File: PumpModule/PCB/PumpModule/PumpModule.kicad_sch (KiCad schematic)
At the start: 8 parts, among them J5 Conn_01x04, J6 Conn_01x04, J7 Conn_01x03

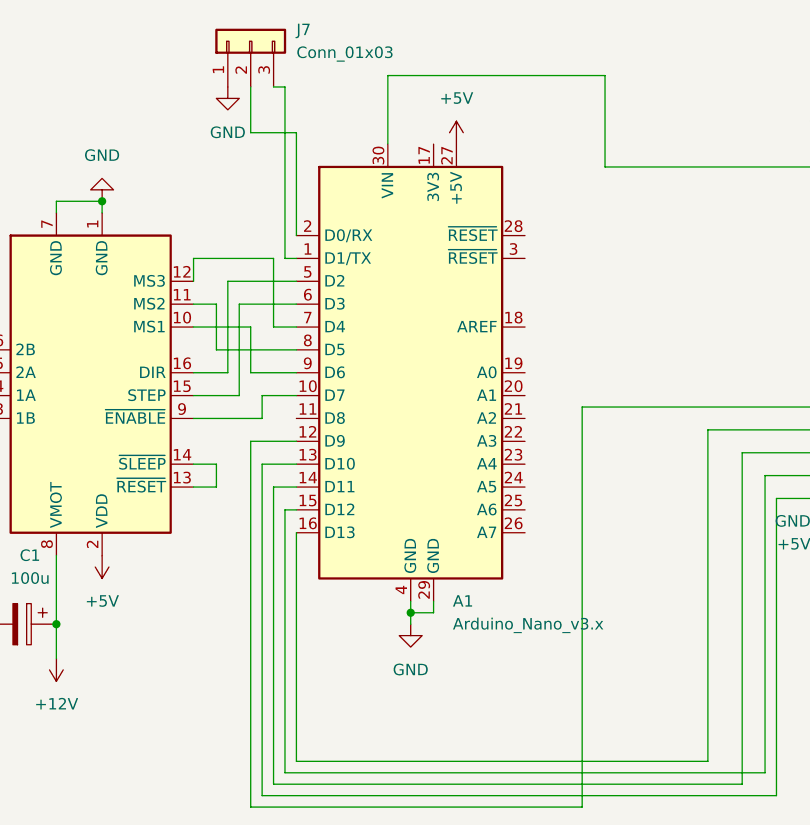
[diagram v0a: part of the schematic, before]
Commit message: [PCB][Pump Module] Fixed PCB pinout
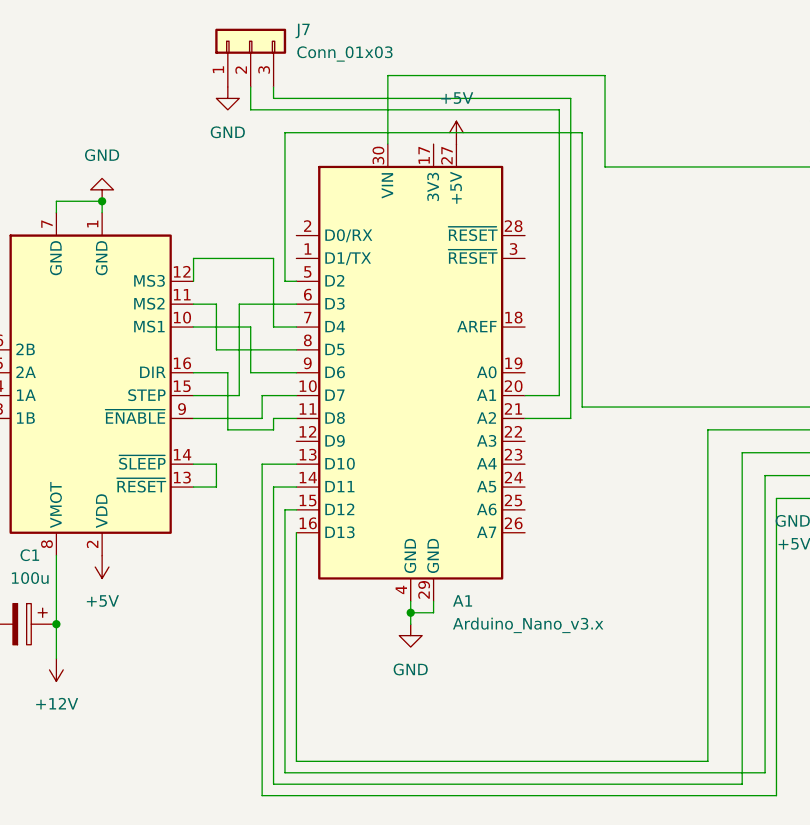
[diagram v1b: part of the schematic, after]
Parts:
- MCP2515Module1, U1: value ~ -> (none)
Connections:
- net at A2.16 (DIR): now also A1.11 (D8); no longer A1.5 (D2)
- net at A1.1 (D1/TX): no longer J7.3 (Pin_3)
- net at A1.12 (D9): no longer MCP2515Module1.7 (INT)
- net at A1.2 (D0/RX): no longer J7.2 (Pin_2)
- net at A1.20 (A1): now also J7.2 (Pin_2)
- net at A1.21 (A2): now also J7.3 (Pin_3)
- new net: A1.5 (D2), MCP2515Module1.7 (INT)

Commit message: [PCB] Made Pump v1.0 PCB
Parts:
- added D1: LED, LED_THT:LED_D2.0mm_W4.8mm_H2.5mm_FlatTop, symbol Device:LED
- added R1: R, Resistor_THT:R_Axial_DIN0204_L3.6mm_D1.6mm_P7.62mm_Horizontal, symbol Device:R
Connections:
- net GND: now also J7.3 (Pin_3), D1.1 (K); no longer J7.1 (Pin_1)
- net at A1.12 (D9): now also R1.1
- net at A1.21 (A2): now also J7.1 (Pin_1); no longer J7.3 (Pin_3)
- new net: D1.2 (A), R1.2

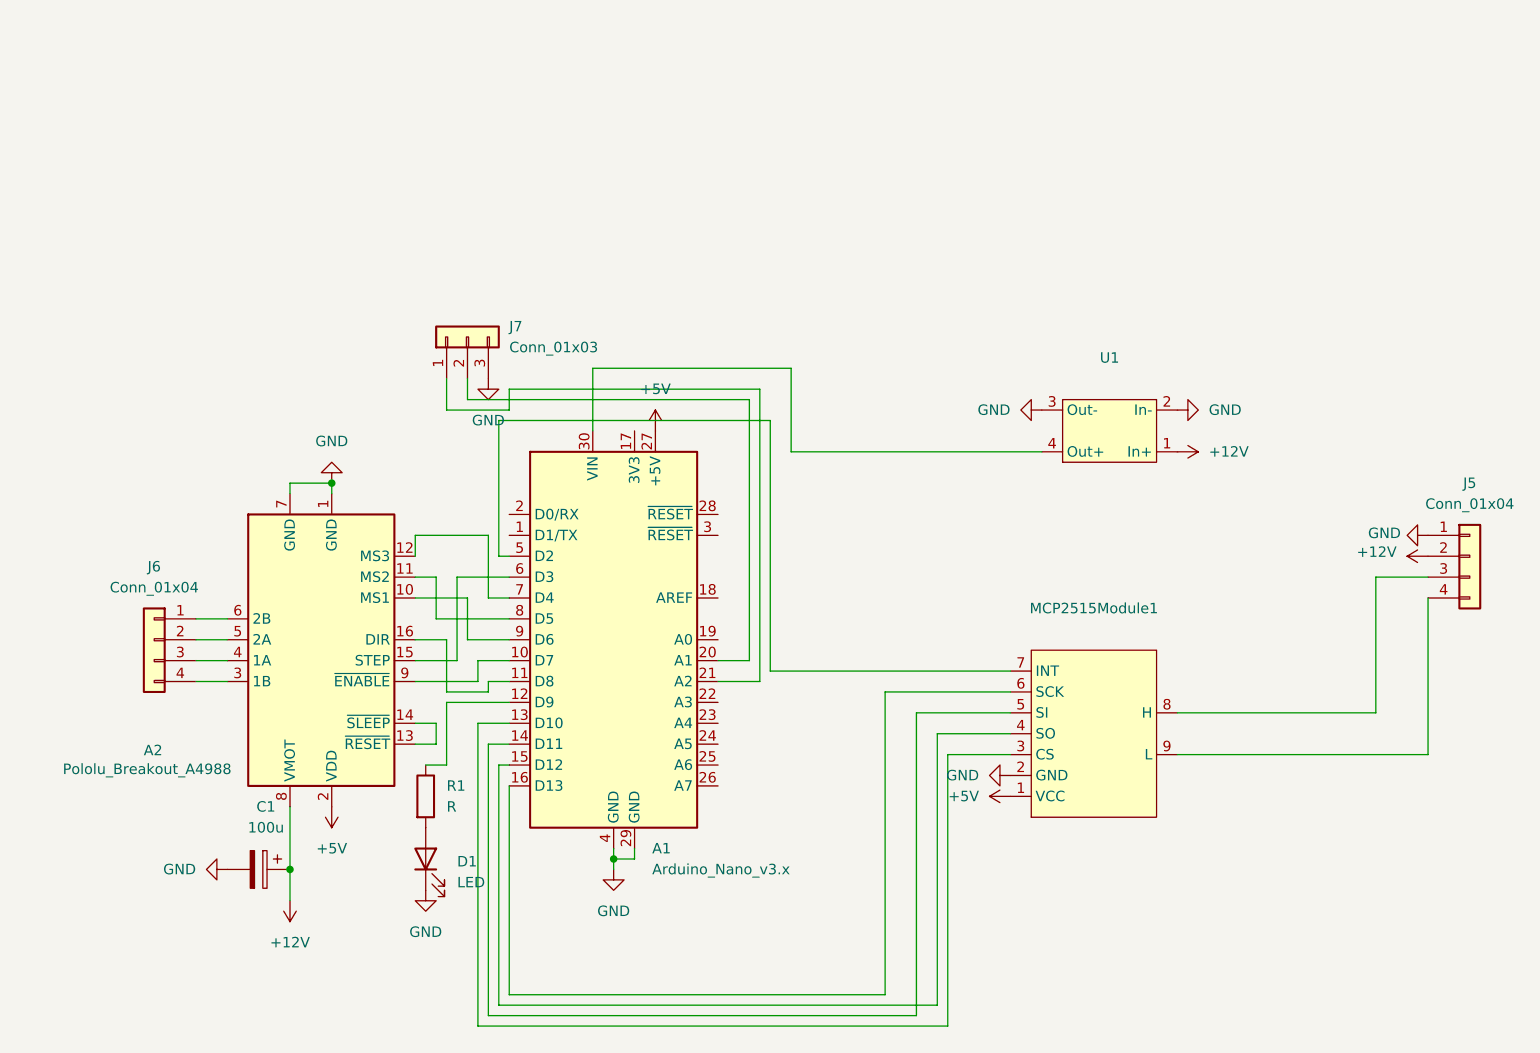
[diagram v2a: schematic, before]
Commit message: [PCB][PumpModule] Fixed input power pinout. Changed indication pin and add status LED to A0 pin
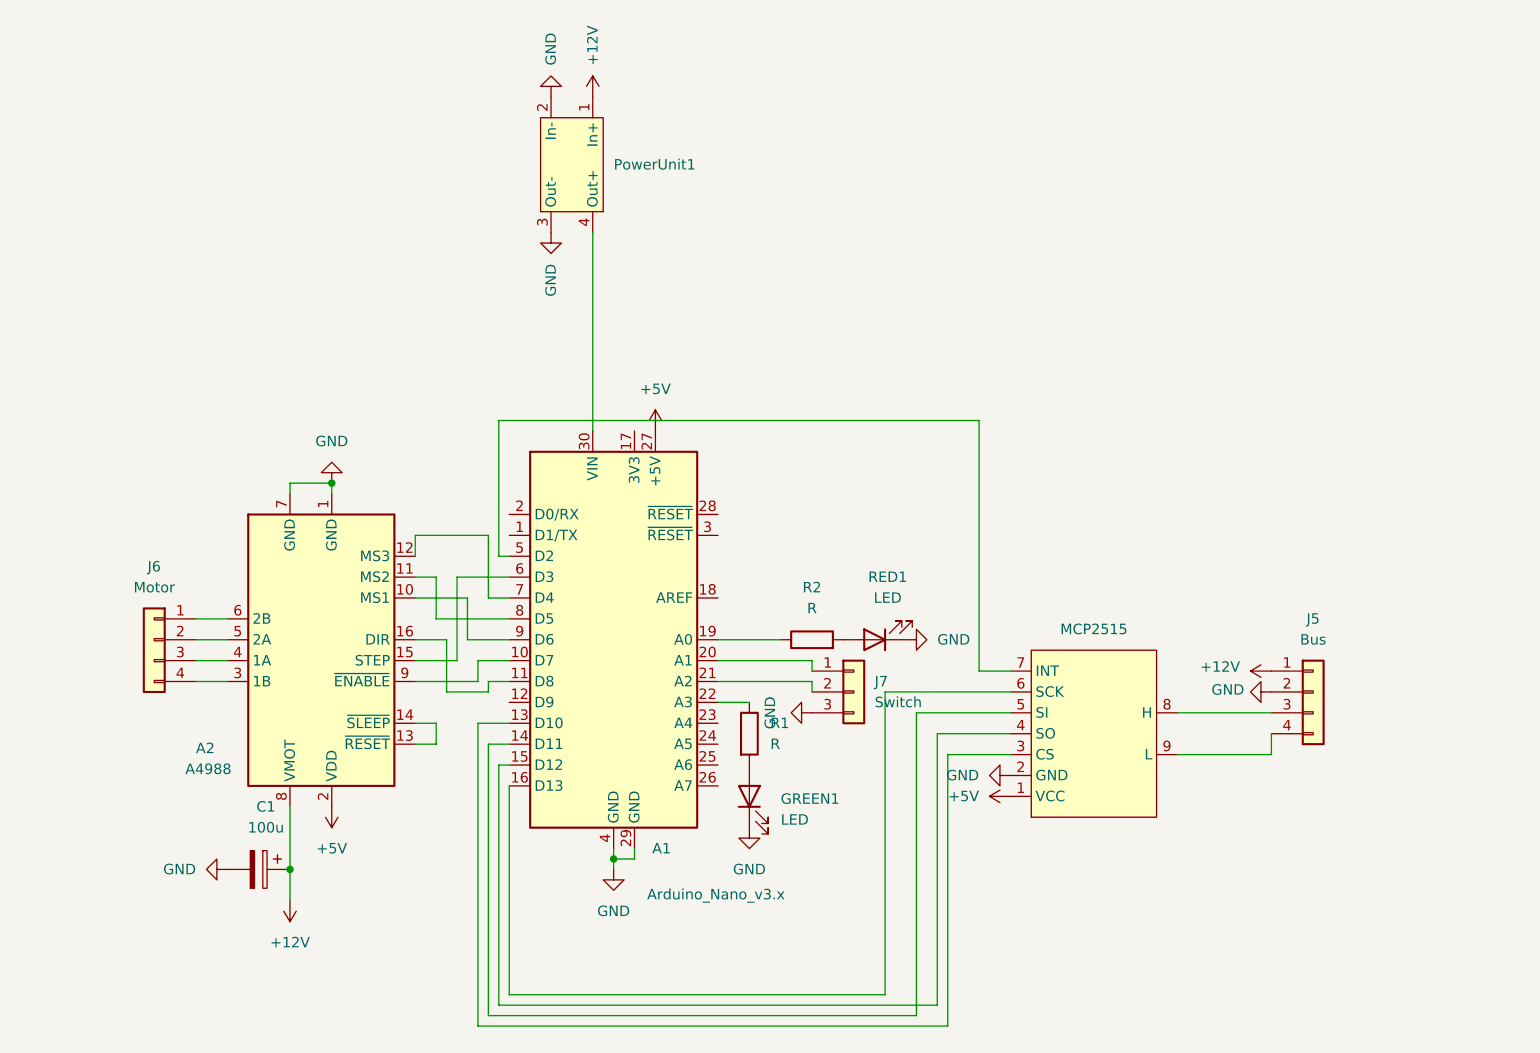
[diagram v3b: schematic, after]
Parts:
- added R2: R, Resistor_SMD:R_0805_2012Metric_Pad1.20x1.40mm_HandSolder, symbol Device:R
- added RED1: LED, LED_SMD:LED_0805_2012Metric, symbol Device:LED
- A2: value Pololu_Breakout_A4988 -> A4988
- GREEN1: renamed from D1; footprint LED_THT:LED_D2.0mm_W4.8mm_H2.5mm_FlatTop -> LED_SMD:LED_0805_2012Metric
- J5: value Conn_01x04 -> Bus
- J6: value Conn_01x04 -> Motor
- J7: value Conn_01x03 -> Switch
- R1: footprint Resistor_THT:R_Axial_DIN0204_L3.6mm_D1.6mm_P7.62mm_Horizontal -> Resistor_SMD:R_0805_2012Metric_Pad1.20x1.40mm_HandSolder
- renumbered MCP2515Module1 to MCP2515, U1 to PowerUnit1
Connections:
- net +12V: now also J5.1 (Pin_1); no longer J5.2 (Pin_2)
- net GND: now also J5.2 (Pin_2), RED1.1 (K); no longer J5.1 (Pin_1)
- net at A1.12 (D9): no longer R1.1
- net at A1.19 (A0): now also R2.1
- net at A1.20 (A1): now also J7.1 (Pin_1); no longer J7.2 (Pin_2)
- net at A1.21 (A2): now also J7.2 (Pin_2); no longer J7.1 (Pin_1)
- net at A1.22 (A3): now also R1.1
- new net: R2.2, RED1.2 (A)
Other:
- moved on the sheet: GREEN1, J5, J7, PowerUnit1, R1
